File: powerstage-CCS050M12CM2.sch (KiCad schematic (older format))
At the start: 42 parts, among them J13 CONN_01X01, Q2 CCS050M12CM2, U10 74LVC2G04, U11 TXS0108E

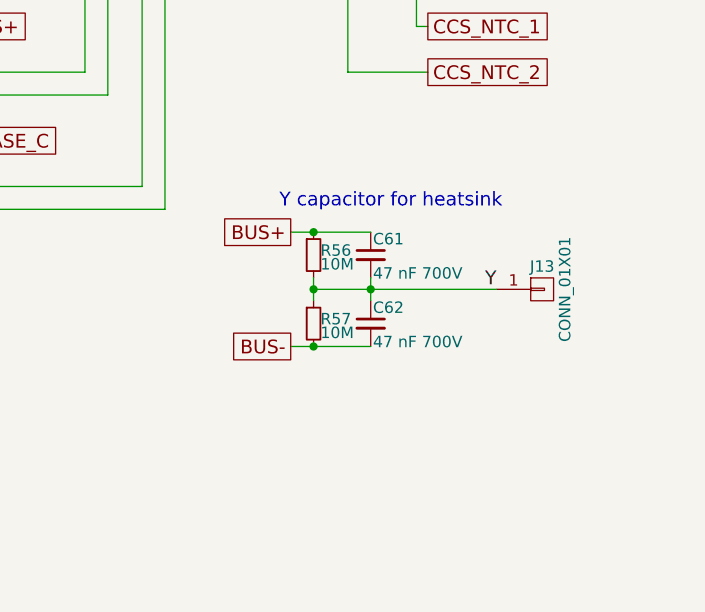
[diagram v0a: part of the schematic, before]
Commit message: Placed AGND plane
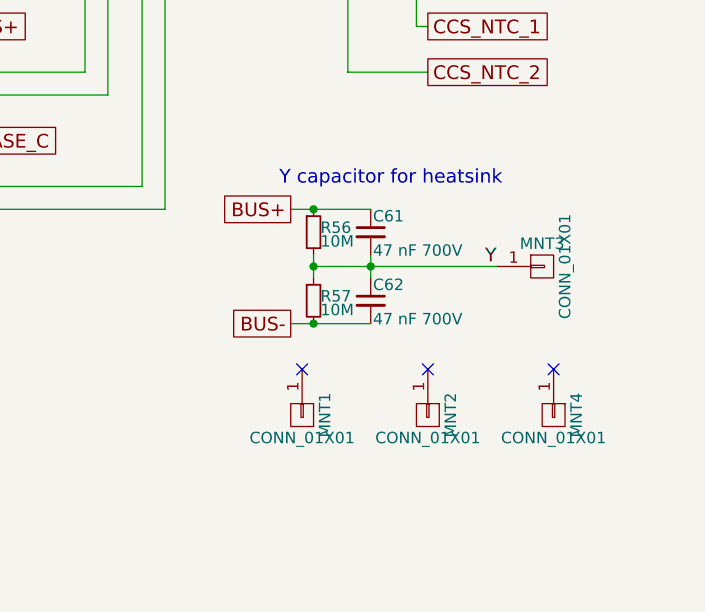
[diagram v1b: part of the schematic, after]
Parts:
- added MNT1, MNT2, MNT4: CONN_01X01, Mounting_Holes:MountingHole_3mm_Pad_Via, symbol CONN_01X01
- MNT3: renamed from J13; footprint Measurement_Points:Measurement_Point_Round-TH_Small -> Mounting_Holes:MountingHole_3mm_Pad_Via
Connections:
- no-connect marks 2 -> 5
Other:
- moved on the sheet: C61, C62, MNT3, R56, R57
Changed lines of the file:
@@
 Text GLabel 9350 5050 2    60   UnSpc ~ 0
 CCS_NTC_2
-Text GLabel 8750 5750 0    60   UnSpc ~ 0
+Text GLabel 8750 5650 0    60   UnSpc ~ 0
 BUS+
-Text GLabel 8750 6250 0    60   UnSpc ~ 0
+Text GLabel 8750 6150 0    60   UnSpc ~ 0
 BUS-
 $Comp
 L C_Small C61
 U 1 1 57FDB526
-P 9100 5850
-F 0 "C61" H 9110 5920 50  0000 L CNN
-F 1 "47 nF 700V" H 9110 5770 50  0000 L CNN
-F 2 "Capacitors_SMD:C_1210" H 9100 5850 50  0001 C CNN
-F 3 "" H 9100 5850 50  0000 C CNN
-	1    9100 5850
+P 9100 5750
+F 0 "C61" H 9110 5820 50  0000 L CNN
+F 1 "47 nF 700V" H 9110 5670 50  0000 L CNN
+F 2 "Capacitors_SMD:C_1210" H 9100 5750 50  0001 C CNN
+F 3 "" H 9100 5750 50  0000 C CNN
+	1    9100 5750
 	1    0    0    -1
 $EndComp
@@
 L R_Small R56
 U 1 1 57FDBE64
-P 8850 5850
-F 0 "R56" H 8880 5870 50  0000 L CNN
-F 1 "10M" H 8880 5810 50  0000 L CNN
-F 2 "Resistors_SMD:R_0805" H 8850 5850 50  0001 C CNN
-F 3 "" H 8850 5850 50  0000 C CNN
-	1    8850 5850
+P 8850 5750
+F 0 "R56" H 8880 5770 50  0000 L CNN
+F 1 "10M" H 8880 5710 50  0000 L CNN
+F 2 "Resistors_SMD:R_0805" H 8850 5750 50  0001 C CNN
+F 3 "" H 8850 5750 50  0000 C CNN
+	1    8850 5750
 	1    0    0    -1
 $EndComp
@@
 L C_Small C62
 U 1 1 57FDCDC0
-P 9100 6150
-F 0 "C62" H 9110 6220 50  0000 L CNN
-F 1 "47 nF 700V" H 9110 6070 50  0000 L CNN
-F 2 "Capacitors_SMD:C_1210" H 9100 6150 50  0001 C CNN
-F 3 "" H 9100 6150 50  0000 C CNN
-	1    9100 6150
+P 9100 6050
+F 0 "C62" H 9110 6120 50  0000 L CNN
+F 1 "47 nF 700V" H 9110 5970 50  0000 L CNN
+F 2 "Capacitors_SMD:C_1210" H 9100 6050 50  0001 C CNN
+F 3 "" H 9100 6050 50  0000 C CNN
+	1    9100 6050
 	1    0    0    -1
 $EndComp
@@
 L R_Small R57
 U 1 1 57FDDE6B
-P 8850 6150
-F 0 "R57" H 8880 6170 50  0000 L CNN
-F 1 "10M" H 8880 6110 50  0000 L CNN
-F 2 "Resistors_SMD:R_0805" H 8850 6150 50  0001 C CNN
-F 3 "" H 8850 6150 50  0000 C CNN
-	1    8850 6150
-	1    0    0    -1
-$EndComp
-$Comp
-L CONN_01X01 J13
+P 8850 6050
+F 0 "R57" H 8880 6070 50  0000 L CNN
+F 1 "10M" H 8880 6010 50  0000 L CNN
+F 2 "Resistors_SMD:R_0805" H 8850 6050 50  0001 C CNN
+F 3 "" H 8850 6050 50  0000 C CNN
+	1    8850 6050
+	1    0    0    -1
+$EndComp
+$Comp
+L CONN_01X01 MNT3
 U 1 1 57FE17BD
-P 9850 6000
-F 0 "J13" H 9850 6100 50  0000 C CNN
-F 1 "CONN_01X01" V 9950 6000 50  0000 C CNN
-F 2 "Measurement_Points:Measurement_Point_Round-TH_Small" H 9850 6000 50  0001 C CNN
-F 3 "" H 9850 6000 50  0000 C CNN
-	1    9850 6000
-	1    0    0    -1
-$EndComp
-Text Notes 8700 5650 0    60   ~ 0
+P 9850 5900
+F 0 "MNT3" H 9850 6000 50  0000 C CNN
+F 1 "CONN_01X01" V 9950 5900 50  0000 C CNN
+F 2 "Mounting_Holes:MountingHole_3mm_Pad_Via" H 9850 5900 50  0001 C CNN
+F 3 "" H 9850 5900 50  0000 C CNN
+	1    9850 5900
+	1    0    0    -1
+$EndComp
+Text Notes 8700 5550 0    60   ~ 0
 Y capacitor for heatsink
 $Comp
@@
 	9000 5050 9000 4700
 Wire Wire Line
-	9100 5950 9100 6050
-Wire Wire Line
-	8850 5950 8850 6050
-Wire Wire Line
-	8850 6000 9650 6000
-Connection ~ 9100 6000
-Connection ~ 8850 6000
-Wire Wire Line
-	8750 5750 9100 5750
-Connection ~ 8850 5750
-Wire Wire Line
-	8750 6250 9100 6250
-Connection ~ 8850 6250
+	9100 5850 9100 5950
+Wire Wire Line
+	8850 5850 8850 5950
+Wire Wire Line
+	8850 5900 9650 5900
+Connection ~ 9100 5900
+Connection ~ 8850 5900
+Wire Wire Line
+	8750 5650 9100 5650
+Connection ~ 8850 5650
+Wire Wire Line
+	8750 6150 9100 6150
+Connection ~ 8850 6150
 Wire Wire Line
 	3250 4250 3250 4550
-Text Label 9600 6000 0    60   ~ 0
+Text Label 9600 5900 0    60   ~ 0
 Y
 Wire Wire Line
@@
 	1    0    0    -1
 $EndComp
+$Comp
+L CONN_01X01 MNT1
+U 1 1 580494E3
+P 8800 6550
+F 0 "MNT1" H 8800 6650 50  0000 C CNN
+F 1 "CONN_01X01" V 8900 6550 50  0000 C CNN
+F 2 "Mounting_Holes:MountingHole_3mm_Pad_Via" H 8800 6550 50  0001 C CNN
+F 3 "" H 8800 6550 50  0000 C CNN
+	1    8800 6550
+	0    1    1    0
+$EndComp
+$Comp
+L CONN_01X01 MNT2
+U 1 1 5804A0FB
+P 9350 6550
+F 0 "MNT2" H 9350 6650 50  0000 C CNN
+F 1 "CONN_01X01" V 9450 6550 50  0000 C CNN
+F 2 "Mounting_Holes:MountingHole_3mm_Pad_Via" H 9350 6550 50  0001 C CNN
+F 3 "" H 9350 6550 50  0000 C CNN
+	1    9350 6550
+	0    1    1    0
+$EndComp
+$Comp
+L CONN_01X01 MNT4
+U 1 1 5804A292
+P 9900 6550
+F 0 "MNT4" H 9900 6650 50  0000 C CNN
+F 1 "CONN_01X01" V 10000 6550 50  0000 C CNN
+F 2 "Mounting_Holes:MountingHole_3mm_Pad_Via" H 9900 6550 50  0001 C CNN
+F 3 "" H 9900 6550 50  0000 C CNN
+	1    9900 6550
+	0    1    1    0
+$EndComp
+NoConn ~ 9900 6350
+NoConn ~ 9350 6350
+NoConn ~ 8800 6350
 $EndSCHEMATC

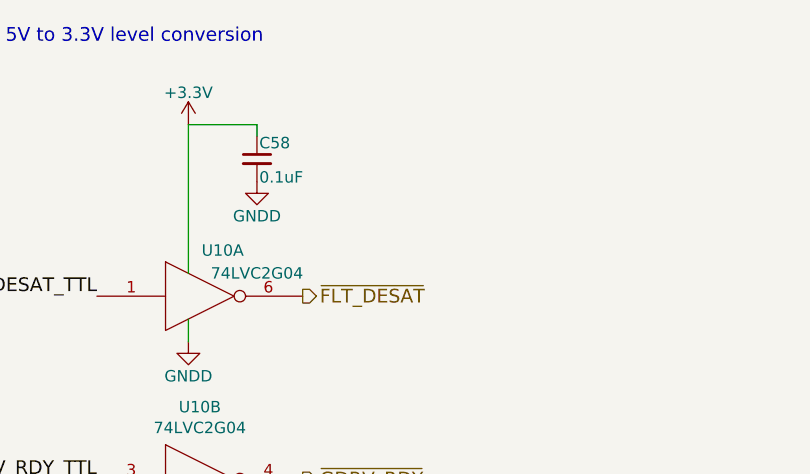
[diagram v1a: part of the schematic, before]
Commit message: further routing; add fault LED
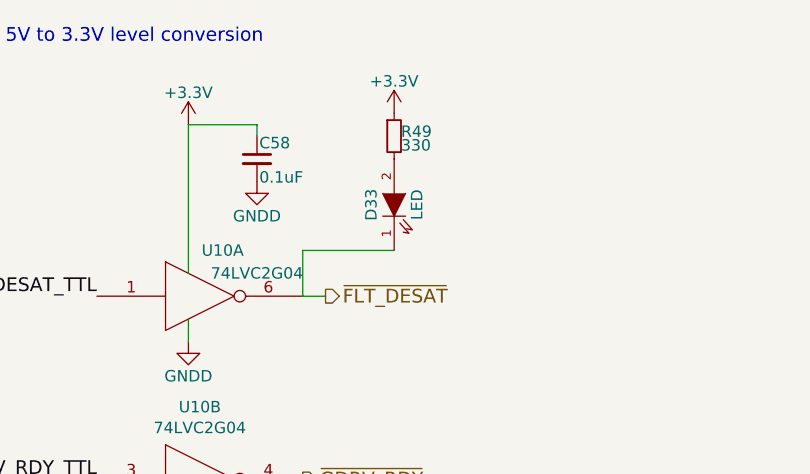
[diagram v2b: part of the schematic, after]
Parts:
- added D33: LED, LEDs:LED_0603, symbol LED
- added R49: 330, Resistors_SMD:R_0402, symbol R_Small
- MNT1, MNT2, MNT3, MNT4: footprint Mounting_Holes:MountingHole_3mm_Pad_Via -> sictroller:MountingHole_3mm_Pad_Via
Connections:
- net +3V3: now also R49.1
- net ~FLT_DESAT: now also D33.1 (K)
- new net: D33.2 (A), R49.2
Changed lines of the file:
@@
 	1    0    0    -1
 $EndComp
-Text HLabel 2700 1950 2    60   Output ~ 0
+Text HLabel 2800 1950 2    60   Output ~ 0
 ~FLT_DESAT
 Text HLabel 2700 2750 2    60   Output ~ 0
@@
 F 0 "MNT3" H 9850 6000 50  0000 C CNN
 F 1 "CONN_01X01" V 9950 5900 50  0000 C CNN
-F 2 "Mounting_Holes:MountingHole_3mm_Pad_Via" H 9850 5900 50  0001 C CNN
+F 2 "sictroller:MountingHole_3mm_Pad_Via" H 9850 5900 50  0001 C CNN
 F 3 "" H 9850 5900 50  0000 C CNN
 	1    9850 5900
@@
 F 0 "MNT1" H 8800 6650 50  0000 C CNN
 F 1 "CONN_01X01" V 8900 6550 50  0000 C CNN
-F 2 "Mounting_Holes:MountingHole_3mm_Pad_Via" H 8800 6550 50  0001 C CNN
+F 2 "sictroller:MountingHole_3mm_Pad_Via" H 8800 6550 50  0001 C CNN
 F 3 "" H 8800 6550 50  0000 C CNN
 	1    8800 6550
@@
 F 0 "MNT2" H 9350 6650 50  0000 C CNN
 F 1 "CONN_01X01" V 9450 6550 50  0000 C CNN
-F 2 "Mounting_Holes:MountingHole_3mm_Pad_Via" H 9350 6550 50  0001 C CNN
+F 2 "sictroller:MountingHole_3mm_Pad_Via" H 9350 6550 50  0001 C CNN
 F 3 "" H 9350 6550 50  0000 C CNN
 	1    9350 6550
@@
 F 0 "MNT4" H 9900 6650 50  0000 C CNN
 F 1 "CONN_01X01" V 10000 6550 50  0000 C CNN
-F 2 "Mounting_Holes:MountingHole_3mm_Pad_Via" H 9900 6550 50  0001 C CNN
+F 2 "sictroller:MountingHole_3mm_Pad_Via" H 9900 6550 50  0001 C CNN
 F 3 "" H 9900 6550 50  0000 C CNN
 	1    9900 6550
@@
 NoConn ~ 9350 6350
 NoConn ~ 8800 6350
+$Comp
+L +3.3V #PWR0109
+U 1 1 5808E7F7
+P 3100 1150
+F 0 "#PWR0109" H 3100 1000 50  0001 C CNN
+F 1 "+3.3V" H 3100 1290 50  0000 C CNN
+F 2 "" H 3100 1150 50  0000 C CNN
+F 3 "" H 3100 1150 50  0000 C CNN
+	1    3100 1150
+	1    0    0    -1
+$EndComp
+$Comp
+L R_Small R49
+U 1 1 5808ECA5
+P 3100 1250
+F 0 "R49" H 3130 1270 50  0000 L CNN
+F 1 "330" H 3130 1210 50  0000 L CNN
+F 2 "Resistors_SMD:R_0402" H 3100 1250 50  0001 C CNN
+F 3 "" H 3100 1250 50  0000 C CNN
+	1    3100 1250
+	1    0    0    -1
+$EndComp
+$Comp
+L LED D33
+U 1 1 5808F624
+P 3100 1550
+F 0 "D33" H 3100 1650 50  0000 C CNN
+F 1 "LED" H 3100 1450 50  0000 C CNN
+F 2 "LEDs:LED_0603" H 3100 1550 50  0001 C CNN
+F 3 "" H 3100 1550 50  0000 C CNN
+	1    3100 1550
+	0    -1   -1   0
+$EndComp
+Wire Wire Line
+	3100 1750 2700 1750
+Wire Wire Line
+	2700 1750 2700 1950
+Wire Wire Line
+	2700 1950 2800 1950
 $EndSCHEMATC

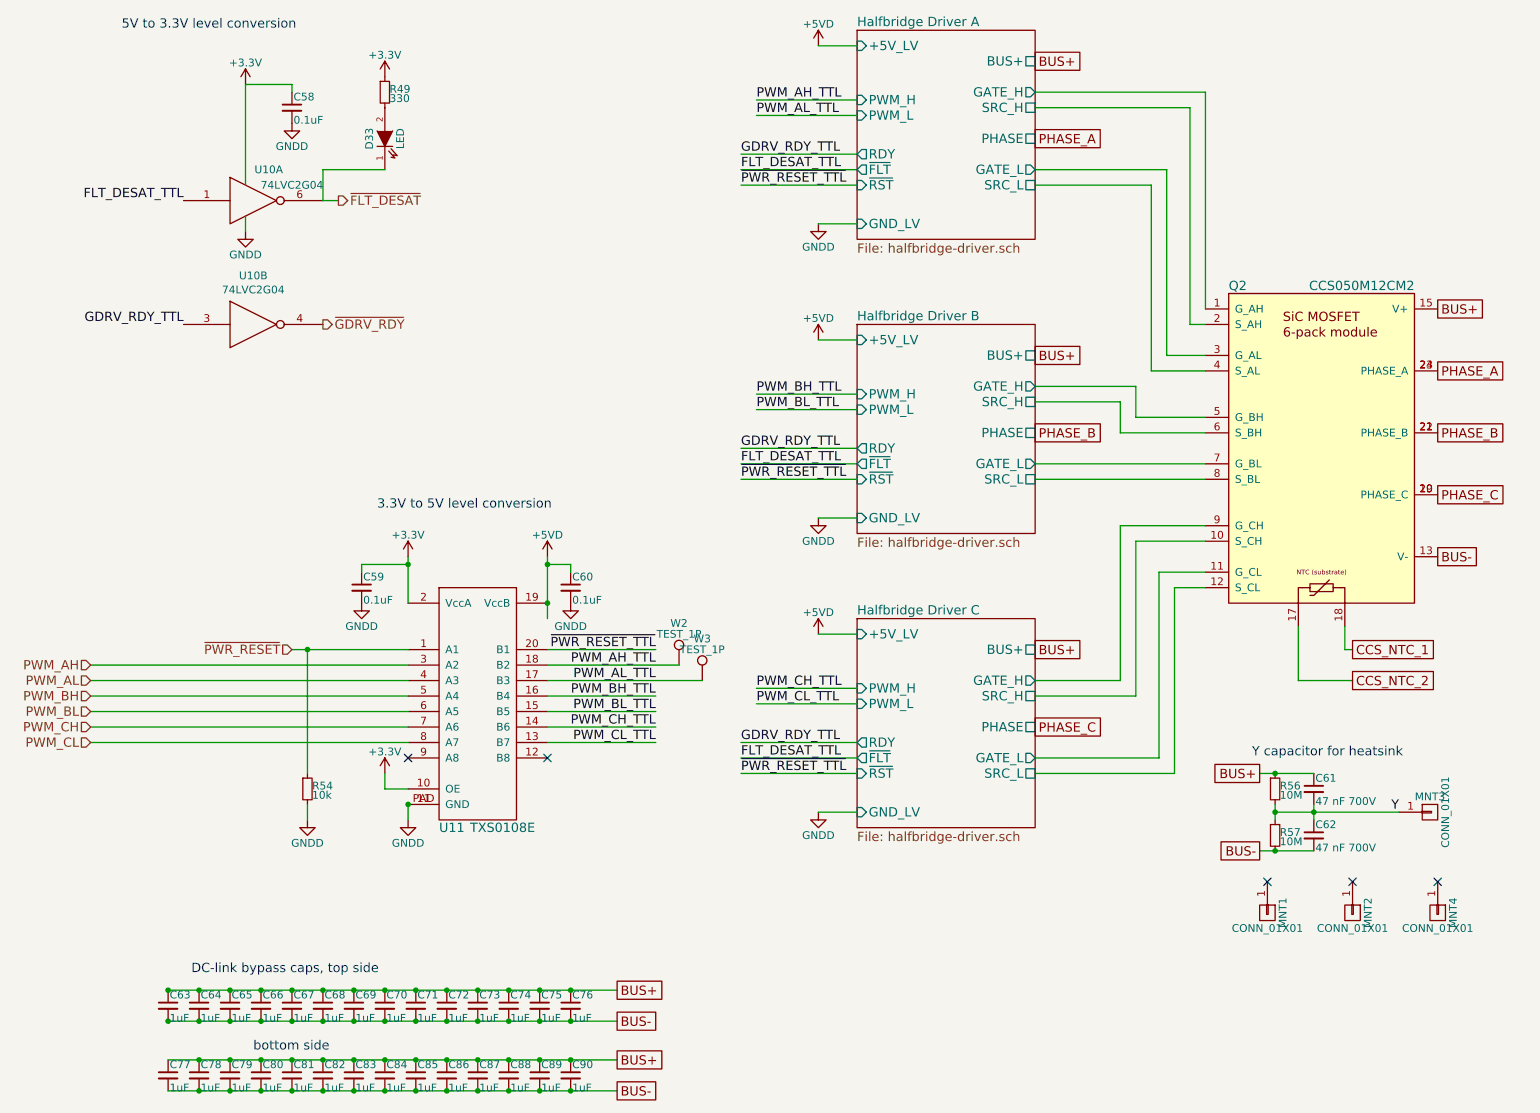
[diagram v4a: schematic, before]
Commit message: V2.1: Fixes for V2.0 bugs
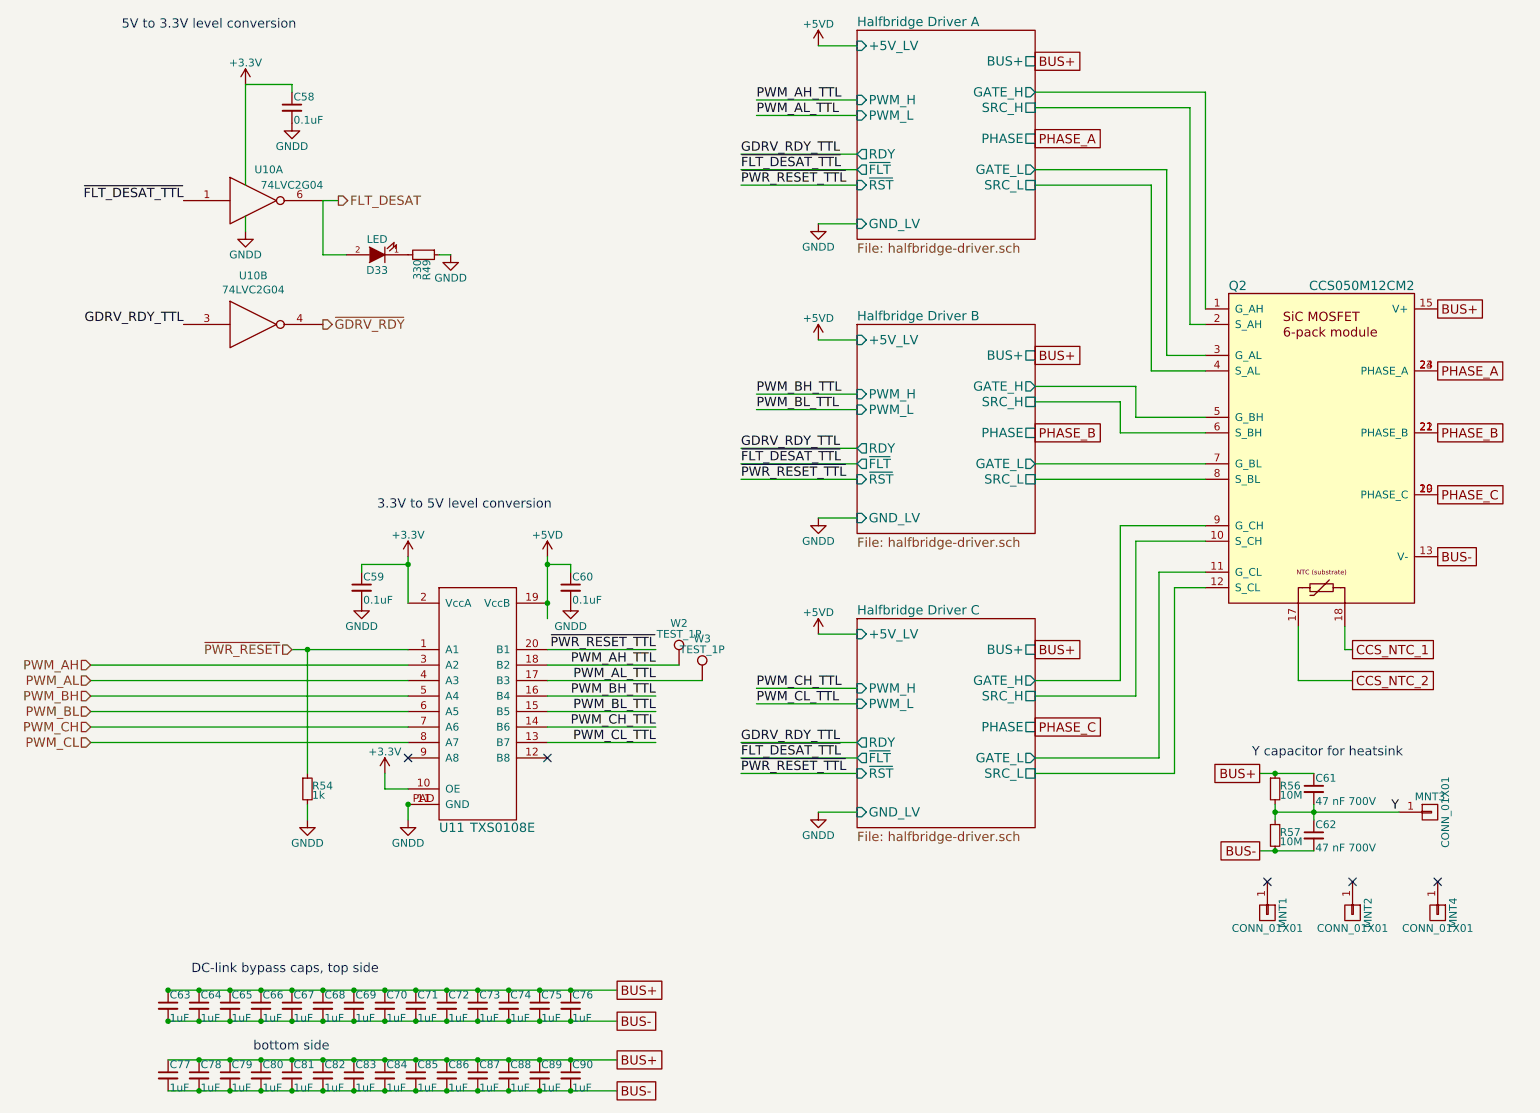
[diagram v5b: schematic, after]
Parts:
- R54: value 10k -> 1k
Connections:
- net +3V3: no longer R49.1
- net GND: now also R49.1
- net at R49.2: now also D33.1 (K); no longer D33.2 (A)
- net FLT_DESAT_TTL renamed ~FLT_DESAT_TTL
- net ~FLT_DESAT renamed FLT_DESAT
- net FLT_DESAT: now also D33.2 (A); no longer D33.1 (K)
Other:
- moved on the sheet: D33, R49
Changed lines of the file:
@@
 $EndComp
 Text Label 1800 1950 2    60   ~ 0
-FLT_DESAT_TTL
+~FLT_DESAT_TTL
 $Comp
 L C_Small C60
@@
 $EndComp
 Text HLabel 2800 1950 2    60   Output ~ 0
-~FLT_DESAT
+FLT_DESAT
 Text HLabel 2700 2750 2    60   Output ~ 0
 ~GDRV_RDY
@@
 GDRV_RDY_TTL
 Text Label 5400 1750 0    60   ~ 0
-FLT_DESAT_TTL
+~FLT_DESAT_TTL
 Text Label 5400 3650 0    60   ~ 0
-FLT_DESAT_TTL
+~FLT_DESAT_TTL
 Text Label 5400 5550 0    60   ~ 0
-FLT_DESAT_TTL
+~FLT_DESAT_TTL
 Text Label 5400 5450 0    60   ~ 0
 GDRV_RDY_TTL
@@
 P 2600 5750
 F 0 "R54" H 2630 5770 50  0000 L CNN
-F 1 "10k" H 2630 5710 50  0000 L CNN
+F 1 "1k" H 2630 5710 50  0000 L CNN
 F 2 "Resistors_SMD:R_0402" H 2600 5750 50  0001 C CNN
 F 3 "" H 2600 5750 50  0000 C CNN
@@
 NoConn ~ 8800 6350
 $Comp
-L +3.3V #PWR0110
-U 1 1 5808E7F7
-P 3100 1150
-F 0 "#PWR0110" H 3100 1000 50  0001 C CNN
-F 1 "+3.3V" H 3100 1290 50  0000 C CNN
-F 2 "" H 3100 1150 50  0000 C CNN
-F 3 "" H 3100 1150 50  0000 C CNN
-	1    3100 1150
-	1    0    0    -1
-$EndComp
-$Comp
 L R_Small R49
 U 1 1 5808ECA5
-P 3100 1250
-F 0 "R49" H 3130 1270 50  0000 L CNN
-F 1 "330" H 3130 1210 50  0000 L CNN
-F 2 "Resistors_SMD:R_0402" H 3100 1250 50  0001 C CNN
-F 3 "" H 3100 1250 50  0000 C CNN
-	1    3100 1250
-	1    0    0    -1
+P 3350 2300
+F 0 "R49" H 3380 2320 50  0000 L CNN
+F 1 "330" H 3380 2260 50  0000 L CNN
+F 2 "Resistors_SMD:R_0402" H 3350 2300 50  0001 C CNN
+F 3 "" H 3350 2300 50  0000 C CNN
+	1    3350 2300
+	0    1    1    0
 $EndComp
 $Comp
 L LED D33
 U 1 1 5808F624
-P 3100 1550
-F 0 "D33" H 3100 1650 50  0000 C CNN
-F 1 "LED" H 3100 1450 50  0000 C CNN
-F 2 "LEDs:LED_0603" H 3100 1550 50  0001 C CNN
-F 3 "" H 3100 1550 50  0000 C CNN
-	1    3100 1550
-	0    -1   -1   0
-$EndComp
-Wire Wire Line
-	3100 1750 2700 1750
-Wire Wire Line
-	2700 1750 2700 1950
+P 3050 2300
+F 0 "D33" H 3050 2400 50  0000 C CNN
+F 1 "LED" H 3050 2200 50  0000 C CNN
+F 2 "LEDs:LED_0603" H 3050 2300 50  0001 C CNN
+F 3 "" H 3050 2300 50  0000 C CNN
+	1    3050 2300
+	-1   0    0    1
+$EndComp
 Wire Wire Line
 	2700 1950 2800 1950
+$Comp
+L GNDD #PWR?
+U 1 1 58437DDD
+P 3525 2300
+F 0 "#PWR?" H 3525 2050 50  0001 C CNN
+F 1 "GNDD" H 3525 2150 50  0000 C CNN
+F 2 "" H 3525 2300 50  0000 C CNN
+F 3 "" H 3525 2300 50  0000 C CNN
+	1    3525 2300
+	1    0    0    -1
+$EndComp
+Wire Wire Line
+	3525 2300 3450 2300
+Wire Wire Line
+	2850 2300 2700 2300
+Wire Wire Line
+	2700 2300 2700 1950
 $EndSCHEMATC
